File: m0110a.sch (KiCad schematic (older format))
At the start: 158 parts

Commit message: Add row and column schematic
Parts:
- added D?: D_Small, symbol Device:D_Small
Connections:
- net COL1: now reaches MX?.1
- net COL1: now also MX?.1, MX?.1, MX?.1, MX?.1
- net COL2: now reaches MX?.1
- net COL2: now also MX?.1, MX?.1, MX?.1
- net COL3: now reaches MX?.1
- net COL3: now also MX?.1, MX?.1, MX?.1
- net COL4: now reaches MX?.1
- net COL4: now also MX?.1, MX?.1, MX?.1
- net COL5: now reaches MX?.1
- net COL5: now also MX?.1, MX?.1, MX?.1, MX?.3 (VSS)
- net COL6: now reaches MX?.1
- net COL6: now also MX?.1, MX?.1, MX?.1
- net COL7: now reaches MX?.1
- net COL7: now also MX?.1, MX?.1, MX?.1
- net COL8: now reaches MX?.1
- net COL8: now also MX?.1, MX?.1, MX?.1
- net COL9: now reaches MX?.1
- net COL9: now also MX?.1, MX?.1, MX?.1
- net COL10: now reaches MX?.1
- net COL10: now also MX?.1, MX?.1, MX?.1, MX?.1
- net COL11: now reaches MX?.1
- net COL11: now also MX?.1, MX?.1, MX?.1
- net COL12: now reaches MX?.1
- net COL12: now also MX?.1, MX?.1, MX?.1
- net COL13: now reaches MX?.1
- net COL13: now also MX?.1, MX?.1, MX?.1, MX?.1
- net COL14: now reaches MX?.1
- net COL14: now also MX?.1, MX?.1, MX?.1, MX?.1
- net COL15: now reaches MX?.1
- net COL15: now also MX?.1, MX?.1, MX?.1
- net COL16: now reaches MX?.1
- net COL16: now also MX?.1, MX?.1, MX?.1, MX?.1
- net COL17: now reaches MX?.1
- net COL17: now also MX?.1, MX?.1, MX?.1
- net COL0: now reaches MX?.1
- net COL0: now also MX?.1, MX?.1, MX?.1, MX?.1
- net at MX?.2: now also D?.2 (A) (x26)
- net ROW0: now reaches D?.1 (K), D?.1 (K), D?.1 (K), D?.1 (K), D?.1 (K), D?.1 (K), D?.1 (K), D?.1 (K), D?.1 (K), D?.1 (K), D?.1 (K), D?.1 (K), D?.1 (K), D?.1 (K), D?.1 (K), D?.1 (K), D?.1 (K), D?.1 (K)
- net ROW1: now reaches D?.1 (K), D?.1 (K), D?.1 (K), D?.1 (K), D?.1 (K), D?.1 (K), D?.1 (K), D?.1 (K), D?.1 (K), D?.1 (K), D?.1 (K), D?.1 (K), D?.1 (K), D?.1 (K), D?.1 (K), D?.1 (K), D?.1 (K), D?.1 (K)
- net ROW2: now reaches D?.1 (K), D?.1 (K), D?.1 (K), D?.1 (K), D?.1 (K), D?.1 (K), D?.1 (K), D?.1 (K), D?.1 (K), D?.1 (K), D?.1 (K), D?.1 (K), D?.1 (K), D?.1 (K), D?.1 (K), D?.1 (K), D?.1 (K)
- net ROW3: now reaches D?.1 (K)
- net ROW3: now also D?.1 (K), D?.1 (K), D?.1 (K), D?.1 (K), D?.1 (K), D?.1 (K), D?.1 (K), D?.1 (K), D?.1 (K), D?.1 (K), D?.1 (K), D?.1 (K), D?.1 (K), D?.1 (K), D?.1 (K), D?.1 (K)
- net ROW4: now reaches D?.1 (K)
- net ROW4: now also D?.1 (K), D?.1 (K), D?.1 (K), D?.1 (K), D?.1 (K), D?.1 (K), D?.1 (K), D?.1 (K)
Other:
- moved on the sheet: D?, MX?, U?

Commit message: add rgb led connections left -> right, top -> bottom
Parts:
- added H1: MountingHole_Pad, MountingHole:MountingHole_2.5mm_Pad, symbol Mechanical:MountingHole_Pad
- D1, D10, D11, D12, D13, D14, D15, D16, D17, D18, D19, D2, D20, D21, D22, D23, D24, D25, D26, D27, D28, D29, D3, D30, D31, D32, D33, D34, D35, D36, D37, D38, D39, D4, D40, D41, D42, D43, D44, D45, D46, D47, D48, D49, D5, D50, D51, D52, D53, D54, D55, D56, D57, D58, D59, D6, D60, D61, D62, D63, D64, D65, D66, D67, D68, D69, D7, D70, D71, D72, D73, D74, D75, D76, D77, D78, D79, D8, D9: renamed from D?; footprint (none) -> Diode_SMD:D_SOD-123
- MX1, MX10, MX11, MX13, MX14, MX15, MX16, MX17, MX18, MX19, MX2, MX20, MX21, MX22, MX23, MX24, MX25, MX26, MX27, MX28, MX29, MX3, MX30, MX31, MX32, MX33, MX34, MX35, MX37, MX38, MX39, MX4, MX40, MX41, MX42, MX43, MX44, MX45, MX46, MX47, MX48, MX49, MX5, MX50, MX51, MX52, MX54, MX55, MX56, MX57, MX58, MX59, MX6, MX60, MX61, MX62, MX63, MX64, MX65, MX66, MX67, MX7, MX72, MX73, MX74, MX75, MX78, MX8, MX9: renamed from MX?; footprint (none) -> CherryMX_PCB_KailhSocket_LTST-A683CEGBW:CherryMX_1.00u_PCB_KailhSocket_LTST-A683CEGBW
- MX12, MX36, MX79: renamed from MX?; footprint (none) -> CherryMX_PCB_KailhSocket_LTST-A683CEGBW:CherryMX_1.50u_PCB_KailhSocket_LTST-A683CEGBW
- MX53: renamed from MX?; footprint (none) -> CherryMX_PCB_KailhSocket_LTST-A683CEGBW:CherryMX_1.75u_PCB_KailhSocket_LTST-A683CEGBW
- MX68: renamed from MX?; footprint (none) -> CherryMX_PCB_KailhSocket_LTST-A683CEGBW:CherryMX_1.25u_PCB_KailhSocket_LTST-A683CEGBW
- MX69: renamed from MX?; footprint (none) -> CherryMX_PCB_KailhSocket_LTST-A683CEGBW:CherryMX_2.25u_PCB_KailhSocket_LTST-A683CEGBW
- MX70, MX76, MX77: renamed from MX?; footprint (none) -> CherryMX_PCB_KailhSocket_LTST-A683CEGBW:CherryMX_2.00u_PCB_KailhSocket_LTST-A683CEGBW
- MX71: renamed from MX?; footprint (none) -> CherryMX_PCB_KailhSocket_LTST-A683CEGBW:CherryMX_7.00u_PCB_KailhSocket_LTST-A683CEGBW
- U1: renamed from U?; footprint (none) -> teensy:Teensy2.0++
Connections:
- net at MX15.4 (DIN): now also MX18.5 (DOUT)
- net at MX15.5 (DOUT): now also MX16.4 (DIN)
- net at MX16.5 (DOUT): now also MX10.4 (DIN)
- net at MX10.5 (DOUT): now also MX7.4 (DIN)
- net at MX7.5 (DOUT): now also MX1.4 (DIN)
- net at MX1.5 (DOUT): now also MX2.4 (DIN)
- net at MX2.5 (DOUT): now also MX3.4 (DIN)
- net at MX3.5 (DOUT): now also MX4.4 (DIN)
- net at MX4.5 (DOUT): now also MX5.4 (DIN)
- net at MX5.5 (DOUT): now also MX6.4 (DIN)
- net at MX6.5 (DOUT): now also MX11.4 (DIN)
- net at MX11.5 (DOUT): now also MX17.4 (DIN)
- net at MX17.5 (DOUT): now also MX12.4 (DIN)
- net at MX12.5 (DOUT): now also MX8.4 (DIN)
- net at MX8.5 (DOUT): now also MX13.4 (DIN)
- net at MX13.5 (DOUT): now also MX9.4 (DIN)
- net at MX9.5 (DOUT): now also MX14.4 (DIN)
- net RGB0: now reaches MX14.5 (DOUT)
- net RGB0: now also MX36.4 (DIN)
- net at MX36.5 (DOUT): now also MX33.4 (DIN)
- net at MX33.5 (DOUT): now also MX34.4 (DIN)
- net at MX34.5 (DOUT): now also MX28.4 (DIN)
- net at MX28.5 (DOUT): now also MX25.4 (DIN)
- net at MX25.5 (DOUT): now also MX19.4 (DIN)
- net at MX19.5 (DOUT): now also MX20.4 (DIN)
- net at MX20.5 (DOUT): now also MX21.4 (DIN)
- net at MX21.5 (DOUT): now also MX22.4 (DIN)
- net at MX22.5 (DOUT): now also MX23.4 (DIN)
- net at MX23.5 (DOUT): now also MX24.4 (DIN)
- net at MX24.5 (DOUT): now also MX29.4 (DIN)
- net at MX29.5 (DOUT): now also MX35.4 (DIN)
- net at MX35.5 (DOUT): now also MX30.4 (DIN)
- net at MX30.5 (DOUT): now also MX26.4 (DIN)
- net at MX26.5 (DOUT): now also MX31.4 (DIN)
- net at MX31.5 (DOUT): now also MX27.4 (DIN)
- net at MX27.5 (DOUT): now also MX32.4 (DIN)
- net RGB1: now reaches MX32.5 (DOUT)
- net RGB1: now also MX53.4 (DIN)
- net at MX53.5 (DOUT): now also MX51.4 (DIN)
- net at MX51.5 (DOUT): now also MX52.4 (DIN)
- net at MX52.5 (DOUT): now also MX46.4 (DIN)
- net at MX46.5 (DOUT): now also MX43.4 (DIN)
- net at MX43.5 (DOUT): now also MX38.4 (DIN)
- net at MX38.5 (DOUT): now also MX39.4 (DIN)
- net at MX39.5 (DOUT): now also MX37.4 (DIN)
- net at MX37.5 (DOUT): now also MX40.4 (DIN)
- net at MX40.5 (DOUT): now also MX41.4 (DIN)
- net at MX41.5 (DOUT): now also MX42.4 (DIN)
- net at MX42.5 (DOUT): now also MX47.4 (DIN)
- net at MX47.5 (DOUT): now also MX48.4 (DIN)
- net at MX48.5 (DOUT): now also MX44.4 (DIN)
- net at MX44.5 (DOUT): now also MX49.4 (DIN)
- net at MX49.5 (DOUT): now also MX45.4 (DIN)
- net at MX45.5 (DOUT): now also MX50.4 (DIN)
- net RGB2: now reaches MX50.5 (DOUT)
- net RGB2: now also MX69.4 (DIN)
- net at MX69.5 (DOUT): now also MX66.4 (DIN)
- net at MX66.5 (DOUT): now also MX67.4 (DIN)
- net at MX67.5 (DOUT): now also MX64.4 (DIN)
- net at MX64.5 (DOUT): now also MX60.4 (DIN)
- net at MX60.5 (DOUT): now also MX55.4 (DIN)
- net at MX55.5 (DOUT): now also MX56.4 (DIN)
- net at MX56.5 (DOUT): now also MX54.4 (DIN)
- net at MX54.5 (DOUT): now also MX57.4 (DIN)
- net at MX57.5 (DOUT): now also MX58.4 (DIN)
- net at MX58.5 (DOUT): now also MX59.4 (DIN)
- net at MX59.5 (DOUT): now also MX68.4 (DIN)
- net at MX68.5 (DOUT): now also MX61.4 (DIN)
- net at MX61.5 (DOUT): now also MX62.4 (DIN)
- net at MX62.5 (DOUT): now also MX65.4 (DIN)
- net at MX65.5 (DOUT): now also MX63.4 (DIN)
- net at MX63.5 (DOUT): now also MX70.4 (DIN)
- net RGB3: now reaches MX70.5 (DOUT)
- net RGB3: now also MX79.4 (DIN)
- net at MX79.5 (DOUT): now also MX77.4 (DIN)
- net at MX77.5 (DOUT): now also MX71.4 (DIN)
- net at MX71.5 (DOUT): now also MX72.4 (DIN)
- net at MX72.5 (DOUT): now also MX74.4 (DIN)
- net at MX74.5 (DOUT): now also MX78.4 (DIN)
- net at MX78.5 (DOUT): now also MX75.4 (DIN)
- net at MX75.5 (DOUT): now also MX76.4 (DIN)
- net at MX76.5 (DOUT): now also MX73.4 (DIN)
- net at MX73.5 (DOUT): now also H1.1
- net GND: now reaches U1.1 (GND)
- net GND: now also U1.22 (GND), U1.33 (GND)
- net VCC: now reaches U1.21 (VCC)

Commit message: fix foot print associations. place switch foot prints and some diodes
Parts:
- MX48: footprint CherryMX_PCB_KailhSocket_LTST-A683CEGBW:CherryMX_1.00u_PCB_KailhSocket_LTST-A683CEGBW -> CherryMX_PCB_KailhSocket_LTST-A683CEGBW:CherryMX_1.75u_PCB_KailhSocket_LTST-A683CEGBW
- MX69: footprint CherryMX_PCB_KailhSocket_LTST-A683CEGBW:CherryMX_2.25u_PCB_KailhSocket_LTST-A683CEGBW -> CherryMX_PCB_KailhSocket_StabWireBottom_LTST-A683CEGBW:CherryMX_2.25u_PCB_KailhSocket_StabWireBottom_LTST-A683CEGBW
- MX70, MX76, MX77: footprint CherryMX_PCB_KailhSocket_LTST-A683CEGBW:CherryMX_2.00u_PCB_KailhSocket_LTST-A683CEGBW -> CherryMX_PCB_KailhSocket_StabWireBottom_LTST-A683CEGBW:CherryMX_2.00u_PCB_KailhSocket_StabWireBottom_LTST-A683CEGBW
- MX71: footprint CherryMX_PCB_KailhSocket_LTST-A683CEGBW:CherryMX_7.00u_PCB_KailhSocket_LTST-A683CEGBW -> CherryMX_PCB_KailhSocket_StabWireBottom_LTST-A683CEGBW:CherryMX_7.00u_PCB_KailhSocket_StabWireBottom_LTST-A683CEGBW
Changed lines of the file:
@@
 F 0 "MX48" H 18930 3089 50  0000 C CNN
 F 1 "CherryMX_LTST-A683CEGBW" H 18930 3006 39  0000 C CNN
-F 2 "CherryMX_PCB_KailhSocket_LTST-A683CEGBW:CherryMX_1.00u_PCB_KailhSocket_LTST-A683CEGBW" H 18930 2620 50  0001 C CNN
+F 2 "CherryMX_PCB_KailhSocket_LTST-A683CEGBW:CherryMX_1.75u_PCB_KailhSocket_LTST-A683CEGBW" H 18930 2620 50  0001 C CNN
 F 3 "" H 18930 2620 50  0001 C CNN
 	1    18930 2720
@@
 F 0 "MX69" H 5440 3919 50  0000 C CNN
 F 1 "CherryMX_LTST-A683CEGBW" H 5440 3836 39  0000 C CNN
-F 2 "CherryMX_PCB_KailhSocket_LTST-A683CEGBW:CherryMX_2.25u_PCB_KailhSocket_LTST-A683CEGBW" H 5440 3450 50  0001 C CNN
+F 2 "CherryMX_PCB_KailhSocket_StabWireBottom_LTST-A683CEGBW:CherryMX_2.25u_PCB_KailhSocket_StabWireBottom_LTST-A683CEGBW" H 5440 3450 50  0001 C CNN
 F 3 "" H 5440 3450 50  0001 C CNN
 	1    5440 3550
@@
 F 0 "MX70" H 24260 4149 50  0000 C CNN
 F 1 "CherryMX_LTST-A683CEGBW" H 24260 4066 39  0000 C CNN
-F 2 "CherryMX_PCB_KailhSocket_LTST-A683CEGBW:CherryMX_2.00u_PCB_KailhSocket_LTST-A683CEGBW" H 24260 3680 50  0001 C CNN
+F 2 "CherryMX_PCB_KailhSocket_StabWireBottom_LTST-A683CEGBW:CherryMX_2.00u_PCB_KailhSocket_StabWireBottom_LTST-A683CEGBW" H 24260 3680 50  0001 C CNN
 F 3 "" H 24260 3680 50  0001 C CNN
 	1    24260 3780
@@
 F 0 "MX77" H 6510 4589 50  0000 C CNN
 F 1 "CherryMX_LTST-A683CEGBW" H 6510 4506 39  0000 C CNN
-F 2 "CherryMX_PCB_KailhSocket_LTST-A683CEGBW:CherryMX_2.00u_PCB_KailhSocket_LTST-A683CEGBW" H 6510 4120 50  0001 C CNN
+F 2 "CherryMX_PCB_KailhSocket_StabWireBottom_LTST-A683CEGBW:CherryMX_2.00u_PCB_KailhSocket_StabWireBottom_LTST-A683CEGBW" H 6510 4120 50  0001 C CNN
 F 3 "" H 6510 4120 50  0001 C CNN
 	1    6510 4220
@@
 F 0 "MX71" H 10730 4559 50  0000 C CNN
 F 1 "CherryMX_LTST-A683CEGBW" H 10730 4476 39  0000 C CNN
-F 2 "CherryMX_PCB_KailhSocket_LTST-A683CEGBW:CherryMX_7.00u_PCB_KailhSocket_LTST-A683CEGBW" H 10730 4090 50  0001 C CNN
+F 2 "CherryMX_PCB_KailhSocket_StabWireBottom_LTST-A683CEGBW:CherryMX_7.00u_PCB_KailhSocket_StabWireBottom_LTST-A683CEGBW" H 10730 4090 50  0001 C CNN
 F 3 "" H 10730 4090 50  0001 C CNN
 	1    10730 4190
@@
 F 0 "MX76" H 21410 4579 50  0000 C CNN
 F 1 "CherryMX_LTST-A683CEGBW" H 21410 4496 39  0000 C CNN
-F 2 "CherryMX_PCB_KailhSocket_LTST-A683CEGBW:CherryMX_2.00u_PCB_KailhSocket_LTST-A683CEGBW" H 21410 4110 50  0001 C CNN
+F 2 "CherryMX_PCB_KailhSocket_StabWireBottom_LTST-A683CEGBW:CherryMX_2.00u_PCB_KailhSocket_StabWireBottom_LTST-A683CEGBW" H 21410 4110 50  0001 C CNN
 F 3 "" H 21410 4110 50  0001 C CNN
 	1    21410 4210

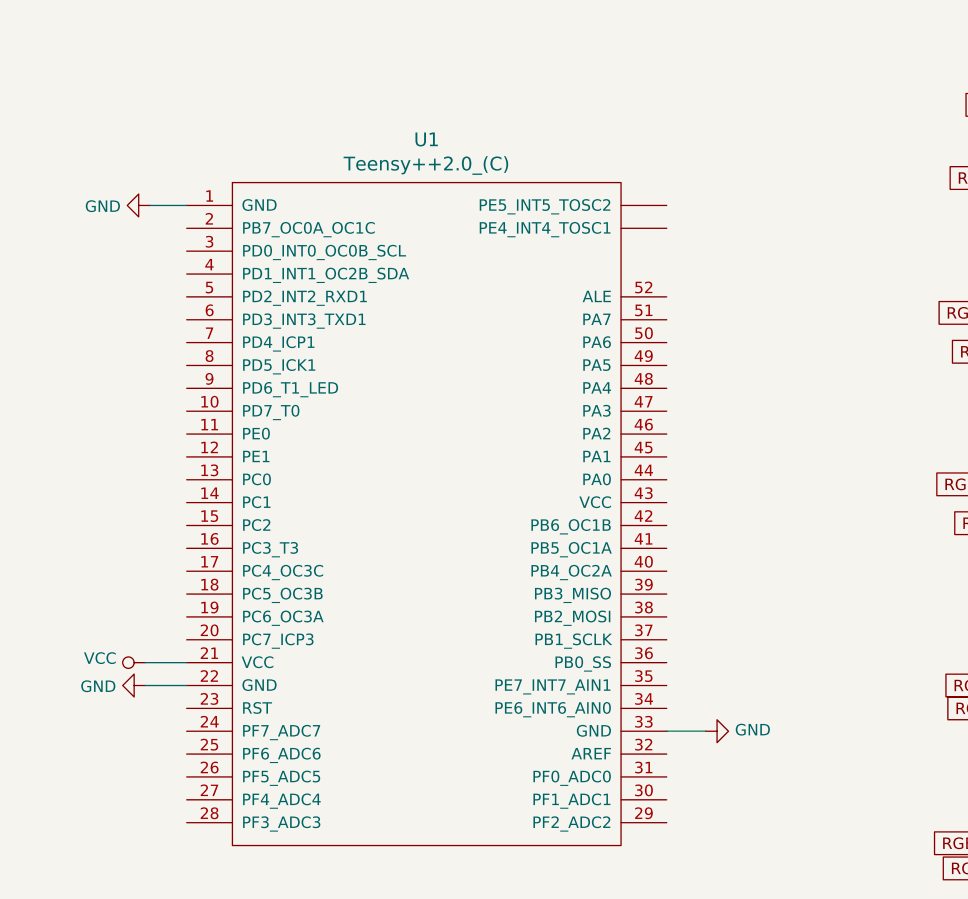
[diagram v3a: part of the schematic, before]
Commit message: add pcb edge cuts
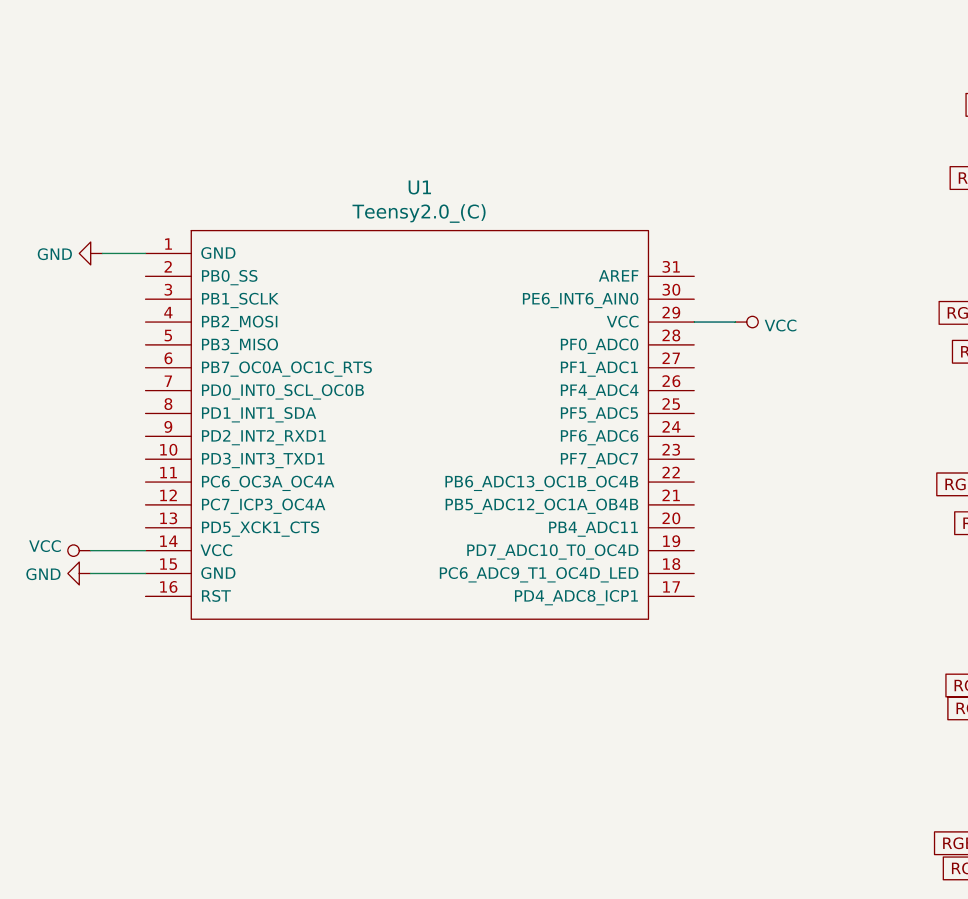
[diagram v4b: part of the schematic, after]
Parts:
- removed U1: Teensy++2.0_(C), teensy:Teensy2.0++, symbol teensy:Teensy++2.0_(C)
- added U1: Teensy2.0_(C), teensy:Teensy2.0, symbol teensy:Teensy2.0_(C)
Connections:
- net GND: now also U1.1 (GND), U1.15 (GND)
- net VCC: now also U1.14 (VCC), U1.29 (VCC)
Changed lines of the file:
@@
 Text GLabel 23880 1060 0    50   Input ~ 0
 COL17
-$Comp
-L teensy:Teensy++2.0_(C) U1
-U 1 1 60AA52E7
-P 2470 2880
-F 0 "U1" H 2470 4517 60  0000 C CNN
-F 1 "Teensy++2.0_(C)" H 2470 4411 60  0000 C CNN
-F 2 "teensy:Teensy2.0++" H 2570 2030 60  0001 C CNN
-F 3 "" H 2570 2030 60  0000 C CNN
-	1    2470 2880
-	1    0    0    -1
-$EndComp
 Wire Wire Line
 	5750 1190 6190 1190
@@
 	24050 4240 24170 4240
 $Comp
+L teensy:Teensy2.0_(C) U1
+U 1 1 62D42544
+P 2440 2490
+F 0 "U1" H 2440 3527 60  0000 C CNN
+F 1 "Teensy2.0_(C)" H 2440 3421 60  0000 C CNN
+F 2 "teensy:Teensy2.0" H 2540 1440 60  0001 C CNN
+F 3 "" H 2540 1440 60  0000 C CNN
+	1    2440 2490
+	1    0    0    -1
+$EndComp
+$Comp
 L power:GND #PWR0101
-U 1 1 6284BDD9
-P 3690 3830
-F 0 "#PWR0101" H 3690 3580 50  0001 C CNN
-F 1 "GND" V 3695 3702 50  0000 R CNN
-F 2 "" H 3690 3830 50  0001 C CNN
-F 3 "" H 3690 3830 50  0001 C CNN
-	1    3690 3830
+U 1 1 62D44A06
+P 1050 1740
+F 0 "#PWR0101" H 1050 1490 50  0001 C CNN
+F 1 "GND" V 1055 1612 50  0000 R CNN
+F 2 "" H 1050 1740 50  0001 C CNN
+F 3 "" H 1050 1740 50  0001 C CNN
+	1    1050 1740
+	0    1    1    0
+$EndComp
+Wire Wire Line
+	1050 1740 1240 1740
+$Comp
+L power:GND #PWR0102
+U 1 1 62DD32FC
+P 1000 3140
+F 0 "#PWR0102" H 1000 2890 50  0001 C CNN
+F 1 "GND" V 1005 3012 50  0000 R CNN
+F 2 "" H 1000 3140 50  0001 C CNN
+F 3 "" H 1000 3140 50  0001 C CNN
+	1    1000 3140
+	0    1    1    0
+$EndComp
+Wire Wire Line
+	1000 3140 1240 3140
+$Comp
+L power:VCC #PWR0103
+U 1 1 62E6314F
+P 1000 3040
+F 0 "#PWR0103" H 1000 2890 50  0001 C CNN
+F 1 "VCC" V 1018 3167 50  0000 L CNN
+F 2 "" H 1000 3040 50  0001 C CNN
+F 3 "" H 1000 3040 50  0001 C CNN
+	1    1000 3040
 	0    -1   -1   0
 $EndComp
 Wire Wire Line
-	3690 3830 3520 3830
+	1000 3040 1240 3040
 $Comp
-L power:GND #PWR0102
-U 1 1 628DAEA3
-P 1240 3630
-F 0 "#PWR0102" H 1240 3380 50  0001 C CNN
-F 1 "GND" V 1245 3502 50  0000 R CNN
-F 2 "" H 1240 3630 50  0001 C CNN
-F 3 "" H 1240 3630 50  0001 C CNN
-	1    1240 3630
+L power:VCC #PWR0104
+U 1 1 62EF450D
+P 3820 2040
+F 0 "#PWR0104" H 3820 1890 50  0001 C CNN
+F 1 "VCC" V 3837 2168 50  0000 L CNN
+F 2 "" H 3820 2040 50  0001 C CNN
+F 3 "" H 3820 2040 50  0001 C CNN
+	1    3820 2040
 	0    1    1    0
 $EndComp
 Wire Wire Line
-	1240 3630 1420 3630
-$Comp
-L power:VCC #PWR0103
-U 1 1 629FC137
-P 1240 3530
-F 0 "#PWR0103" H 1240 3380 50  0001 C CNN
-F 1 "VCC" V 1258 3657 50  0000 L CNN
-F 2 "" H 1240 3530 50  0001 C CNN
-F 3 "" H 1240 3530 50  0001 C CNN
-	1    1240 3530
-	0    -1   -1   0
-$EndComp
-Wire Wire Line
-	1240 3530 1420 3530
-$Comp
-L power:GND #PWR0104
-U 1 1 62A8C3A5
-P 1260 1530
-F 0 "#PWR0104" H 1260 1280 50  0001 C CNN
-F 1 "GND" V 1265 1402 50  0000 R CNN
-F 2 "" H 1260 1530 50  0001 C CNN
-F 3 "" H 1260 1530 50  0001 C CNN
-	1    1260 1530
-	0    1    1    0
-$EndComp
-Wire Wire Line
-	1260 1530 1420 1530
+	3820 2040 3640 2040
 $EndSCHEMATC

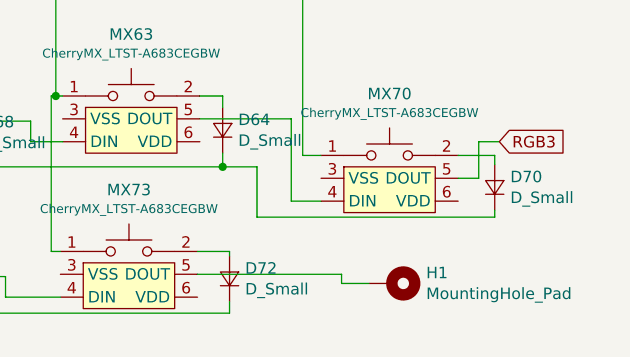
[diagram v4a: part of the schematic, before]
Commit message: connect first row diodes and rgb data lines
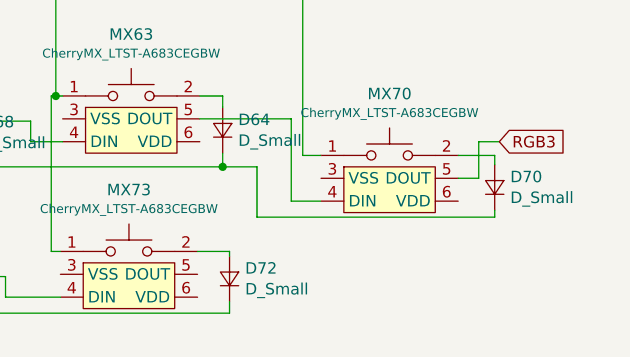
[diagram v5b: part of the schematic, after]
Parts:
- removed H1: MountingHole_Pad, MountingHole:MountingHole_2.5mm_Pad, symbol Mechanical:MountingHole_Pad
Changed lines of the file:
@@
 	22580 4300 22820 4300
-$Comp
-L Mechanical:MountingHole_Pad H1
-U 1 1 627BD20C
-P 24270 4240
-F 0 "H1" V 24224 4390 50  0000 L CNN
-F 1 "MountingHole_Pad" V 24315 4390 50  0000 L CNN
-F 2 "MountingHole:MountingHole_2.5mm_Pad" H 24270 4240 50  0001 C CNN
-F 3 "~" H 24270 4240 50  0001 C CNN
-	1    24270 4240
-	0    1    1    0
-$EndComp
-Wire Wire Line
-	23420 4200 24050 4200
-Wire Wire Line
-	24050 4200 24050 4240
-Wire Wire Line
-	24050 4240 24170 4240
 $Comp
 L teensy:Teensy2.0_(C) U1

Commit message: add column connections
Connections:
- net COL10: now also MX74.1; no longer MX72.1
- net COL11: now also MX68.1, MX78.1; no longer MX74.1
- net COL12: no longer MX68.1, MX78.1
- net COL5: now also MX55.1; no longer MX55.3 (VSS)
- net COL9: now also MX72.1
- net ROW4: now also U1.17 (PD4_ADC8_ICP1)
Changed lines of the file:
@@
-$EndComp
-$Comp
-L CherryMX:CherryMX_LTST-A683CEGBW MX55
-U 1 1 5F470B27
-P 10740 3510
-F 0 "MX55" H 10740 3879 50  0000 C CNN
-F 1 "CherryMX_LTST-A683CEGBW" H 10740 3796 39  0000 C CNN
-F 2 "CherryMX_PCB_KailhSocket_LTST-A683CEGBW:CherryMX_1.00u_PCB_KailhSocket_LTST-A683CEGBW" H 10740 3410 50  0001 C CNN
-F 3 "" H 10740 3410 50  0001 C CNN
-	1    10740 3510
-	1    0    0    -1
 $EndComp
 $Comp
@@
 	10430 4090 10390 4090
 Wire Wire Line
-	10390 4090 10390 3510
-Wire Wire Line
-	10390 3510 10440 3510
-Wire Wire Line
-	10390 3510 10390 2600
-Wire Wire Line
 	10390 2600 10440 2600
-Connection ~ 10390 3510
 Wire Wire Line
 	10390 2600 10390 1860
@@
 Connection ~ 15500 2600
 Wire Wire Line
-	15500 3410 15500 4090
-Wire Wire Line
-	15500 4090 15520 4090
-Connection ~ 15500 3410
-Wire Wire Line
-	16640 4110 16600 4110
-Wire Wire Line
-	16600 4110 16600 2620
-Wire Wire Line
 	16600 2620 16650 2620
 Wire Wire Line
@@
 Wire Wire Line
 	16600 1880 16660 1880
-Connection ~ 16600 2620
 Wire Wire Line
 	16600 1880 16600 1070
@@
 	17780 1890 17820 1890
 Wire Wire Line
-	17780 1890 17780 3090
-Wire Wire Line
-	17780 3090 17390 3090
-Wire Wire Line
 	17390 3090 17390 3440
 Wire Wire Line
 	17390 3440 17430 3440
-Connection ~ 17780 1890
 Wire Wire Line
 	17390 3440 17390 4120
@@
 Wire Wire Line
 	3820 2040 3640 2040
+Text GLabel 3640 3240 2    39   Input ~ 0
+ROW4
+$Comp
+L CherryMX:CherryMX_LTST-A683CEGBW MX55
+U 1 1 5F470B27
+P 10740 3510
+F 0 "MX55" H 10740 3879 50  0000 C CNN
+F 1 "CherryMX_LTST-A683CEGBW" H 10740 3796 39  0000 C CNN
+F 2 "CherryMX_PCB_KailhSocket_LTST-A683CEGBW:CherryMX_1.00u_PCB_KailhSocket_LTST-A683CEGBW" H 10740 3410 50  0001 C CNN
+F 3 "" H 10740 3410 50  0001 C CNN
+	1    10740 3510
+	1    0    0    -1
+$EndComp
+Wire Wire Line
+	10390 2600 10390 3410
+Wire Wire Line
+	10440 3410 10390 3410
+Connection ~ 10390 3410
+Wire Wire Line
+	10390 3410 10390 4090
+Wire Wire Line
+	14340 4090 14340 3410
+Wire Wire Line
+	14340 4090 15520 4090
+Connection ~ 14340 3410
+Wire Wire Line
+	16330 4110 16330 3790
+Wire Wire Line
+	16330 3790 15500 3790
+Wire Wire Line
+	15500 3790 15500 3410
+Wire Wire Line
+	16330 4110 16640 4110
+Connection ~ 15500 3410
+Wire Wire Line
+	17390 3090 16600 3090
+Wire Wire Line
+	16600 3090 16600 2620
+Connection ~ 16600 2620
 $EndSCHEMATC
